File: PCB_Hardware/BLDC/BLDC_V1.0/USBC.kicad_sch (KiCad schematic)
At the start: 9 parts, among them J11 GT-USB-7010ASV, U10 TPD2E2U06DCK

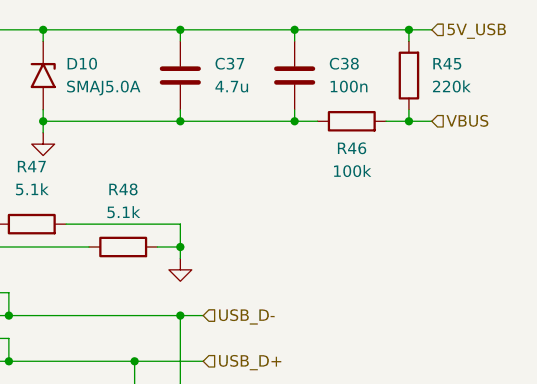
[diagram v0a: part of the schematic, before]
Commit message: redid external temp sensing and instead removed V Bus sense from the USBC input
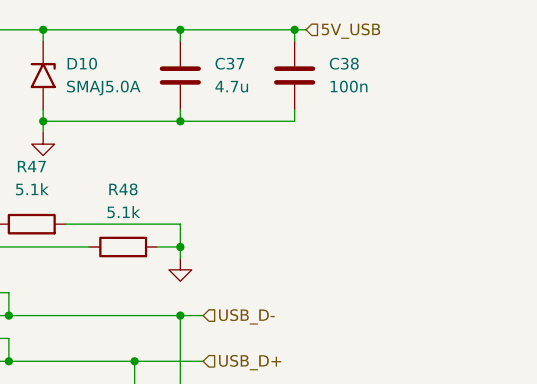
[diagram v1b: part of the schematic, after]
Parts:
- removed R45: 220k, Resistor_SMD:R_0402_1005Metric, symbol Device:R
- removed R46: 100k, Resistor_SMD:R_0402_1005Metric, symbol Device:R
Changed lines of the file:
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@@
-	)
-	(junction
-		(at 177.8 64.77)
-		(diameter 0)
-		(color 0 0 0 0)
 	)
 	(junction
@@
 	)
 	(junction
-		(at 165.1 74.93)
-		(diameter 0)
-		(color 0 0 0 0)
-	)
-	(junction
 		(at 107.95 120.65)
-		(diameter 0)
-		(color 0 0 0 0)
-	)
-	(junction
-		(at 177.8 74.93)
 		(diameter 0)
 		(color 0 0 0 0)
@@
 	(wire
 		(pts
-			(xy 165.1 74.93) (xy 167.64 74.93)
-		)
-		(stroke
-			(width 0)
-			(type default)
-		)
-	)
-	(wire
-		(pts
 			(xy 132.08 64.77) (xy 137.16 64.77)
 		)
@@
 	(wire
 		(pts
-			(xy 177.8 66.04) (xy 177.8 64.77)
-		)
-		(stroke
-			(width 0)
-			(type default)
-		)
-	)
-	(wire
-		(pts
 			(xy 137.16 64.77) (xy 137.16 66.04)
 		)
@@
 	(wire
 		(pts
-			(xy 175.26 74.93) (xy 177.8 74.93)
-		)
-		(stroke
-			(width 0)
-			(type default)
-		)
-	)
-	(wire
-		(pts
 			(xy 130.81 93.98) (xy 133.35 93.98)
 		)
@@
 	(wire
 		(pts
-			(xy 177.8 64.77) (xy 165.1 64.77)
+			(xy 165.1 64.77) (xy 166.37 64.77)
 		)
 		(stroke
@@
 	(wire
 		(pts
-			(xy 177.8 73.66) (xy 177.8 74.93)
-		)
-		(stroke
-			(width 0)
-			(type default)
-		)
-	)
-	(wire
-		(pts
 			(xy 107.95 119.38) (xy 107.95 120.65)
 		)
@@
 		(pts
 			(xy 115.57 120.65) (xy 107.95 120.65)
-		)
-		(stroke
-			(width 0)
-			(type default)
-		)
-	)
-	(wire
-		(pts
-			(xy 177.8 74.93) (xy 180.34 74.93)
-		)
-		(stroke
-			(width 0)
-			(type default)
-		)
-	)
-	(wire
-		(pts
-			(xy 177.8 64.77) (xy 180.34 64.77)
 		)
 		(stroke
@@
 	(hierarchical_label "5V_USB"
 		(shape input)
-		(at 180.34 64.77 0)
+		(at 166.37 64.77 0)
 		(effects
 			(font
@@
 		(shape input)
 		(at 154.94 96.52 0)
-		(effects
-			(font
-				(size 1.27 1.27)
-			)
-			(justify left)
-		)
-	)
-	(hierarchical_label "VBUS"
-		(shape input)
-		(at 180.34 74.93 0)
 		(effects
 			(font
@@
 					(unit 1)
 				)
-			)
-		)
-	)
-	(symbol
-		(lib_id "Device:R")
-		(at 177.8 69.85 180)
-		(unit 1)
-		(body_style 1)
-		(exclude_from_sim no)
-		(in_bom yes)
-		(on_board yes)
-		(in_pos_files yes)
-		(dnp no)
-		(fields_autoplaced yes)
-		(property "Reference" "R45"
-			(at 180.34 68.5799 0)
-			(show_name no)
-			(do_not_autoplace no)
-			(effects
-				(font
-					(size 1.27 1.27)
-				)
-				(justify right)
-			)
-		)
-		(property "Value" "220k"
-			(at 180.34 71.1199 0)
-			(show_name no)
-			(do_not_autoplace no)
-			(effects
-				(font
-					(size 1.27 1.27)
-				)
-				(justify right)
-			)
-		)
-		(property "Footprint" "Resistor_SMD:R_0402_1005Metric"
-			(at 179.578 69.85 90)
-			(hide yes)
-			(show_name no)
-			(do_not_autoplace no)
-			(effects
-				(font
-					(size 1.27 1.27)
-				)
-			)
-		)
-		(property "Datasheet" ""
-			(at 177.8 69.85 0)
-			(hide yes)
-			(show_name no)
-			(do_not_autoplace no)
-			(effects
-				(font
-					(size 1.27 1.27)
-				)
-			)
-		)
-		(property "Description" "Resistor"
-			(at 177.8 69.85 0)
-			(hide yes)
-			(show_name no)
-			(do_not_autoplace no)
-			(effects
-				(font
-					(size 1.27 1.27)
-				)
-			)
-		)
-		(pin "1"
-		)
-		(pin "2"
-		)
-		(instances
-			(project "BLDC_V1.0"
-				(path "/55f9ea03-7b89-4b61-9599-7cac20295fbb/1bfd0788-fffd-4064-ae06-93bfbcdcc4d1"
-					(reference "R45")
-					(unit 1)
-				)
-			)
-		)
-	)
-	(symbol
-		(lib_id "Device:R")
-		(at 171.45 74.93 90)
-		(unit 1)
-		(body_style 1)
-		(exclude_from_sim no)
-		(in_bom yes)
-		(on_board yes)
-		(in_pos_files yes)
-		(dnp no)
-		(property "Reference" "R46"
-			(at 171.45 77.978 90)
-			(show_name no)
-			(do_not_autoplace no)
-			(effects
-				(font
-					(size 1.27 1.27)
-				)
-			)
-		)
-		(property "Value" "100k"
-			(at 171.45 80.518 90)
-			(show_name no)
-			(do_not_autoplace no)
-			(effects
-				(font
-					(size 1.27 1.27)
-				)
-			)
-		)
-		(property "Footprint" "Resistor_SMD:R_0402_1005Metric"
-			(at 171.45 76.708 90)
-			(hide yes)
-			(show_name no)
-			(do_not_autoplace no)
-			(effects
-				(font
-					(size 1.27 1.27)
-				)
-			)
-		)
-		(property "Datasheet" ""
-			(at 171.45 74.93 0)
-			(hide yes)
-			(show_name no)
-			(do_not_autoplace no)
-			(effects
-				(font
-					(size 1.27 1.27)
-				)
-			)
-		)
-		(property "Description" "Resistor"
-			(at 171.45 74.93 0)
-			(hide yes)
-			(show_name no)
-			(do_not_autoplace no)
-			(effects
-				(font
-					(size 1.27 1.27)
-				)
-			)
-		)
-		(pin "1"
-		)
-		(pin "2"
-		)
-		(instances
-			(project "BLDC_V1.0"
-				(path "/55f9ea03-7b89-4b61-9599-7cac20295fbb/1bfd0788-fffd-4064-ae06-93bfbcdcc4d1"
-					(reference "R46")
-					(unit 1)
-				)
